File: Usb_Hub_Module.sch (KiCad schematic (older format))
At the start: 40 parts, among them U1 LAN9514I, U2 IP4220CZ6, X1 ABM3-25.000MHZ-D2Y-T

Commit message: Added logic level shifter on pcb
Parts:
- C1, C7: value 4_7uF_0603 -> 4.7uF/6V3
- C10: value 1uF_0603 -> 1uF/6V3
- C11, C12, C13, C14, C15, C16, C17, C18, C19, C2, C20, C21, C5, C6, C8, C9: value 100nF_0402 -> 100nF/50V
- C22: value 100nF_0603 -> 100nF/50V
- C3, C4: value 30pF_0402 -> 30pF/50V
- R1: value 12k4_0402_1% -> 12k/1%
- R2: value 10k_0402 -> 10k
- R3: value 1M_0402 -> 1M
- R4: value 12k_0402_1% -> 12k/1%
- R5, R6: value 0R_0603 -> 0R
- R7, R8, R9: value 470R_0402 -> 470R
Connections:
- net labels added: POWER_IN_3V3, POWER_IN_GND, POWER_IN_VBUS, USB_D2_OUT_N, USB_D2_OUT_P, USB_D3_OUT_N, USB_D3_OUT_P, USB_D4_OUT_N, USB_D4_OUT_P, USB_D5_OUT_N, USB_D5_OUT_P, USB_HUB_IN_N, USB_HUB_IN_P
- net labels removed: POWER_3V3, POWER_VBUS, USB_EMAR_BOARD_TERMINAL_D+, USB_EMAR_BOARD_TERMINAL_D-, USB_EXTERNAL_D+, USB_EXTERNAL_D-, USB_HUB_COMPUTER_D+, USB_HUB_COMPUTER_D-, USB_MODEM_D+, USB_MODEM_D-, USB_NXP_D+, USB_NXP_D-
- wire segments 107 -> 112
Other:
- note removed: "AUTO-MDIX\n-------------------"
- note removed: "Components C21, C22, C25, C26, C27,C28, C29, C31, C32, C92, C93, U14 are fitted in variants: basic, full, minipcie."
- note removed: "Components from this sheet are fitted in variants: full, minipcie."
- note removed: "Peripheral 2. USB/Ethernet Connector"
- note removed: "Peripheral 3. EMAR Board/Terminal (Removable Port)"
- note removed: "Peripheral 4. NXP (Removable Port)"
- note removed: "Peripheral 5. Modem"
- note removed: "USB Computer ESD protection in "USB_Jumper" sheet."
- note removed: "enabled:\nTX may be swapped internally with RX."

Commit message: Added connection for ethernet modules
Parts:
- removed D2: KPT-1608CGCK, Diodes:LED_KPT-1608CGCK, symbol Diodes:KPT-1608CGCK
- removed D3: KP-1608YC, Diodes:LED_KP-1608YC, symbol Diodes:KP-1608YC
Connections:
- net labels added: LNKA_LED_ANODE, SPD_LED_ANODE, ~LNKA_LED_CATHODE, ~SPD_LED_CATHODE
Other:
- note removed: "GREEN"
- note removed: "YELLOW"
- moved on the sheet: R8, R9
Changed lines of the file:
@@
 	9050 8050 10050 8050
 Wire Wire Line
-	9050 8150 10050 8150
-Wire Wire Line
-	10050 8250 9050 8250
+	9050 8150 9400 8150
+Wire Wire Line
+	9400 8250 9050 8250
 Wire Wire Line
 	11400 8050 11050 8050
 Wire Wire Line
 	10550 8050 10450 8050
-Wire Wire Line
-	10450 8150 10550 8150
-Wire Wire Line
-	11400 8150 11050 8150
-Wire Wire Line
-	10550 8250 10450 8250
-Wire Wire Line
-	11400 8250 11050 8250
 Text Notes 11600 8050 0    50   Italic 10
 RED
-Text Notes 11600 8150 0    50   Italic 10
-GREEN
-Text Notes 11600 8250 0    50   Italic 10
-YELLOW
 Text HLabel 9050 7600 2    50   Output ~ 10
 ETHERNET_TXP
@@
 	1    5900 3450
 	1    0    0    -1
-$EndComp
-$Comp
-L Diodes:KP-1608YC D3
-U 1 1 5CE71DA6
-P 10250 8250
-F 0 "D3" H 10150 8200 50  0000 C CNN
-F 1 "KP-1608YC" H 10850 8200 50  0000 C CNN
-F 2 "Diodes:LED_KP-1608YC" H 10500 7950 50  0001 C CNN
-F 3 "Diodes/Components_Documentation/KP-1608YC.pdf" H 10500 7950 50  0001 C CNN
-F 4 "	KINGBRIGHT ELECTRONIC" H 10250 8250 50  0001 C CNN "Manufacturer"
-F 5 "KP-1608YC" H 10250 8250 50  0001 C CNN "Manufacturer Part Number"
-F 6 "TME" H 10250 8250 50  0001 C CNN "Supplier"
-F 7 "KP-1608YC" H 10250 8250 50  0001 C CNN "Supplier Part Number"
-F 8 "https://www.tme.eu/pl/details/kp-1608yc/diody-led-smd-kolorowe/kingbright-electronic/" H 10250 8250 50  0001 C CNN "URL"
-F 9 "0,4591" H 10250 8250 50  0001 C CNN "Price@1pc"
-F 10 "0,1570" H 10250 8250 50  0001 C CNN "Price@1000pcs"
-F 11 "-basic,+full,+minipcie" H 10250 8250 50  0001 C CNN "Variant"
-F 12 "0603" H 10250 8250 50  0001 C CNN "Package"
-	1    10250 8250
-	-1   0    0    1
-$EndComp
-$Comp
-L Diodes:KPT-1608CGCK D2
-U 1 1 5CED3E4F
-P 10250 8150
-F 0 "D2" H 10150 8100 50  0000 C CNN
-F 1 "KPT-1608CGCK" H 10900 8100 50  0000 C CNN
-F 2 "Diodes:LED_KPT-1608CGCK" H 10250 8150 50  0001 C CNN
-F 3 "Diodes/Components_Documentation/KPT-1608CGCK.pdf" H 10250 8150 50  0001 C CNN
-F 4 "	KINGBRIGHT ELECTRONIC" H 10250 8150 50  0001 C CNN "Manufacturer"
-F 5 "KP-1608CGCK" H 10250 8150 50  0001 C CNN "Manufacturer Part Number"
-F 6 "TME" H 10250 8150 50  0001 C CNN "Supplier"
-F 7 "KP-1608CGCK" H 10250 8150 50  0001 C CNN "Supplier Part Number"
-F 8 "https://www.tme.eu/pl/details/kp-1608cgck/diody-led-smd-kolorowe/kingbright-electronic/" H 10250 8150 50  0001 C CNN "URL"
-F 9 "0,47368" H 10250 8150 50  0001 C CNN "Price@1pc"
-F 10 "0,16283" H 10250 8150 50  0001 C CNN "Price@1000pcs"
-F 11 "WP" H 10250 8150 50  0001 C CNN "Developer"
-F 12 "-basic,+full,+minipcie" H 10250 8150 50  0001 C CNN "Variant"
-F 13 "0603" H 10250 8150 50  0001 C CNN "Package"
-	1    10250 8150
-	-1   0    0    1
 $EndComp
 $Comp
@@
 L Resistors_Smd0402:470R_0402 R8
 U 1 1 5DD6825D
-P 10800 8150
-F 0 "R8" V 10750 7900 50  0000 C CNN
-F 1 "470R" V 10800 8150 50  0000 C CNN
-F 2 "Resistor_Smd_0402:470R_0402" H 11050 7750 50  0001 C CNN
-F 3 "Resistors/Smd_0402/Components_Documentation/crcw0402.pdf" H 11050 7750 50  0001 C CNN
-F 4 "0402" H 10800 8150 50  0001 C CNN "Package"
-F 5 "ROYAL OHM" H 10800 8150 50  0001 C CNN "Manufacturer"
-F 6 "0402WGF4700TCE" H 10800 8150 50  0001 C CNN "Manufacturer Part Number"
-F 7 "TME" H 10800 8150 50  0001 C CNN "Supplier"
-F 8 "SMD0402-470R-1%" H 10800 8150 50  0001 C CNN "Supplier Part Number"
-F 9 "https://www.tme.eu/pl/details/smd0402-470r-1%25/rezystory-smd-0402/royal-ohm/0402wgf4700tce/" H 10800 8150 50  0001 C CNN "URL"
-F 10 "0,0389" H 10800 8150 50  0001 C CNN "Price@1pc"
-F 11 "0,01047" H 10800 8150 50  0001 C CNN "Price@1000pcs"
-F 12 "WP" H 10800 8150 50  0001 C CNN "Developer"
-F 13 "-basic,+full,+minipcie" H 10800 8150 50  0001 C CNN "Variant"
-	1    10800 8150
+P 9650 8150
+F 0 "R8" V 9600 7900 50  0000 C CNN
+F 1 "470R" V 9650 8150 50  0000 C CNN
+F 2 "Resistor_Smd_0402:470R_0402" H 9900 7750 50  0001 C CNN
+F 3 "Resistors/Smd_0402/Components_Documentation/crcw0402.pdf" H 9900 7750 50  0001 C CNN
+F 4 "0402" H 9650 8150 50  0001 C CNN "Package"
+F 5 "ROYAL OHM" H 9650 8150 50  0001 C CNN "Manufacturer"
+F 6 "0402WGF4700TCE" H 9650 8150 50  0001 C CNN "Manufacturer Part Number"
+F 7 "TME" H 9650 8150 50  0001 C CNN "Supplier"
+F 8 "SMD0402-470R-1%" H 9650 8150 50  0001 C CNN "Supplier Part Number"
+F 9 "https://www.tme.eu/pl/details/smd0402-470r-1%25/rezystory-smd-0402/royal-ohm/0402wgf4700tce/" H 9650 8150 50  0001 C CNN "URL"
+F 10 "0,0389" H 9650 8150 50  0001 C CNN "Price@1pc"
+F 11 "0,01047" H 9650 8150 50  0001 C CNN "Price@1000pcs"
+F 12 "WP" H 9650 8150 50  0001 C CNN "Developer"
+F 13 "-basic,+full,+minipcie" H 9650 8150 50  0001 C CNN "Variant"
+	1    9650 8150
 	0    1    1    0
 $EndComp
@@
 L Resistors_Smd0402:470R_0402 R9
 U 1 1 5DD685EA
-P 10800 8250
-F 0 "R9" V 10750 8000 50  0000 C CNN
-F 1 "470R" V 10800 8250 50  0000 C CNN
-F 2 "Resistor_Smd_0402:470R_0402" H 11050 7850 50  0001 C CNN
-F 3 "Resistors/Smd_0402/Components_Documentation/crcw0402.pdf" H 11050 7850 50  0001 C CNN
-F 4 "0402" H 10800 8250 50  0001 C CNN "Package"
-F 5 "ROYAL OHM" H 10800 8250 50  0001 C CNN "Manufacturer"
-F 6 "0402WGF4700TCE" H 10800 8250 50  0001 C CNN "Manufacturer Part Number"
-F 7 "TME" H 10800 8250 50  0001 C CNN "Supplier"
-F 8 "SMD0402-470R-1%" H 10800 8250 50  0001 C CNN "Supplier Part Number"
-F 9 "https://www.tme.eu/pl/details/smd0402-470r-1%25/rezystory-smd-0402/royal-ohm/0402wgf4700tce/" H 10800 8250 50  0001 C CNN "URL"
-F 10 "0,0389" H 10800 8250 50  0001 C CNN "Price@1pc"
-F 11 "0,01047" H 10800 8250 50  0001 C CNN "Price@1000pcs"
-F 12 "WP" H 10800 8250 50  0001 C CNN "Developer"
-F 13 "-basic,+full,+minipcie" H 10800 8250 50  0001 C CNN "Variant"
-	1    10800 8250
+P 9650 8250
+F 0 "R9" V 9600 8000 50  0000 C CNN
+F 1 "470R" V 9650 8250 50  0000 C CNN
+F 2 "Resistor_Smd_0402:470R_0402" H 9900 7850 50  0001 C CNN
+F 3 "Resistors/Smd_0402/Components_Documentation/crcw0402.pdf" H 9900 7850 50  0001 C CNN
+F 4 "0402" H 9650 8250 50  0001 C CNN "Package"
+F 5 "ROYAL OHM" H 9650 8250 50  0001 C CNN "Manufacturer"
+F 6 "0402WGF4700TCE" H 9650 8250 50  0001 C CNN "Manufacturer Part Number"
+F 7 "TME" H 9650 8250 50  0001 C CNN "Supplier"
+F 8 "SMD0402-470R-1%" H 9650 8250 50  0001 C CNN "Supplier Part Number"
+F 9 "https://www.tme.eu/pl/details/smd0402-470r-1%25/rezystory-smd-0402/royal-ohm/0402wgf4700tce/" H 9650 8250 50  0001 C CNN "URL"
+F 10 "0,0389" H 9650 8250 50  0001 C CNN "Price@1pc"
+F 11 "0,01047" H 9650 8250 50  0001 C CNN "Price@1000pcs"
+F 12 "WP" H 9650 8250 50  0001 C CNN "Developer"
+F 13 "-basic,+full,+minipcie" H 9650 8250 50  0001 C CNN "Variant"
+	1    9650 8250
 	0    1    1    0
 $EndComp
@@
 Text Label 11400 8050 0    50   ~ 0
 3V3
-Text Label 11400 8150 0    50   ~ 0
-3V3
-Text Label 11400 8250 0    50   ~ 0
-3V3
 Text Label 12650 5650 0    50   ~ 0
 VBUS
@@
 Text Label 12250 2500 0    50   ~ 0
 3V3
+Wire Wire Line
+	9900 8150 11400 8150
+Wire Wire Line
+	9900 8250 11400 8250
+Text HLabel 11400 8150 2    50   Input ~ 0
+~LNKA_LED_CATHODE
+Text HLabel 11400 8250 2    50   Input ~ 0
+~SPD_LED_CATHODE
+Text HLabel 11400 8400 2    50   Output ~ 0
+LNKA_LED_ANODE
+Text HLabel 11400 8500 2    50   Output ~ 0
+SPD_LED_ANODE
+Text Label 11300 8400 2    50   ~ 0
+3V3
+Text Label 11300 8500 2    50   ~ 0
+3V3
+Wire Wire Line
+	11400 8400 11300 8400
+Wire Wire Line
+	11300 8500 11400 8500
 $EndSCHEMATC

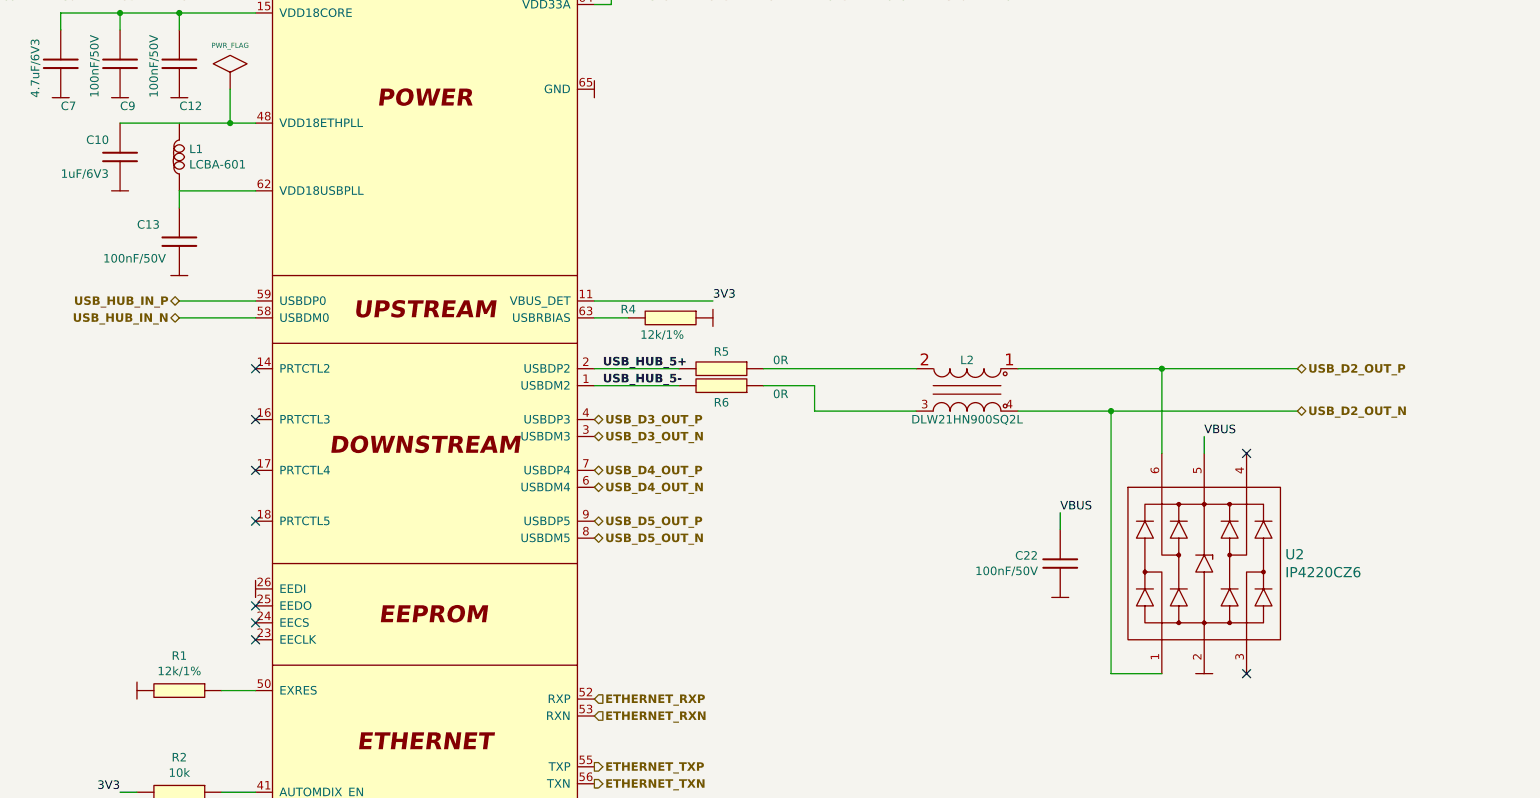
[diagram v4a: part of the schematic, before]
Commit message: Updated README.md and figurated components on pcb
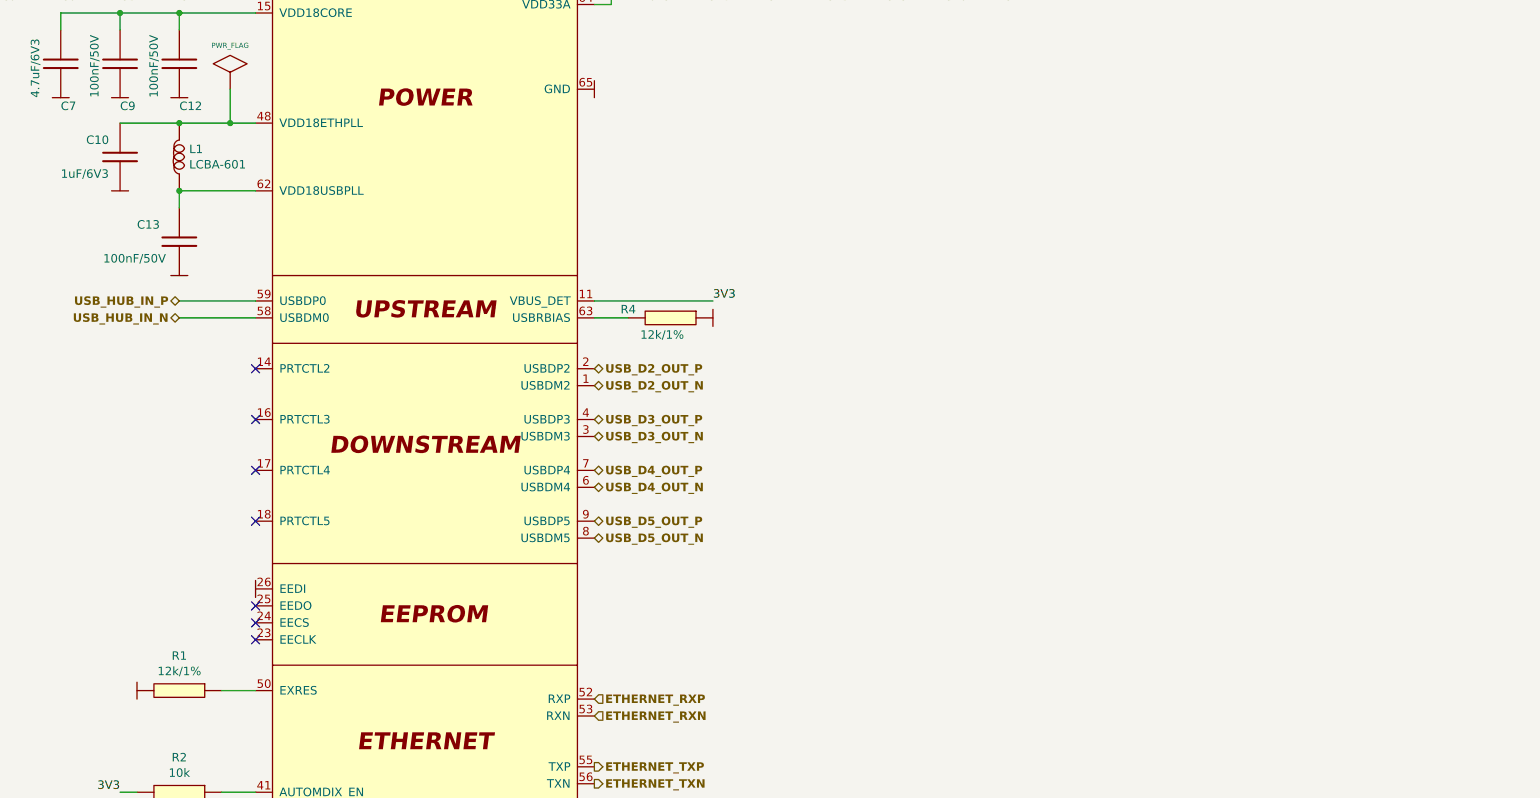
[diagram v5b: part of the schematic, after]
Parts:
- removed C22: 100nF/50V, Capacitors_Smd_0603:100nF_0603, symbol Capacitors_Smd0603:100nF_0603
- removed L2: DLW21HN900SQ2L, Inductors:DLW21HN900SQ2L, symbol Inductors:DLW21HN900SQ2L
- removed R5, R6: 0R, Resistor_Smd_0603:0R_0603, symbol Resistors_Smd0603:0R_0603
- removed U2: IP4220CZ6, ESD_Protectors:IP4220CZ6_SOT457, symbol esd_protectors:IP4220CZ6
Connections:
- net USB_HUB_5+ is gone; now on net USB_D2_OUT_P: U1.2 (USBDP2)
- net USB_HUB_5- is gone; now on net USB_D2_OUT_N: U1.1 (USBDM2)
- net at L1.2: now also C10.1, U1.48 (VDD18ETHPLL)
- no-connect marks 16 -> 14
